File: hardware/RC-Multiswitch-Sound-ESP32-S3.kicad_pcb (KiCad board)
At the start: 2 copper layers, 106 x 68.2 mm, 39 parts, among them CN1 UART A, CN2 3S, CN4 Lautsprecher, J1 Ausgaenge, J11 TPA3118 HW-327, J2 PCM5102A, J5 UART B, J6 UART C, J9 microSD-TF-Modul, U1 ESP32-S3-DevKitC-1 (N16R8), U2 ULN2803A

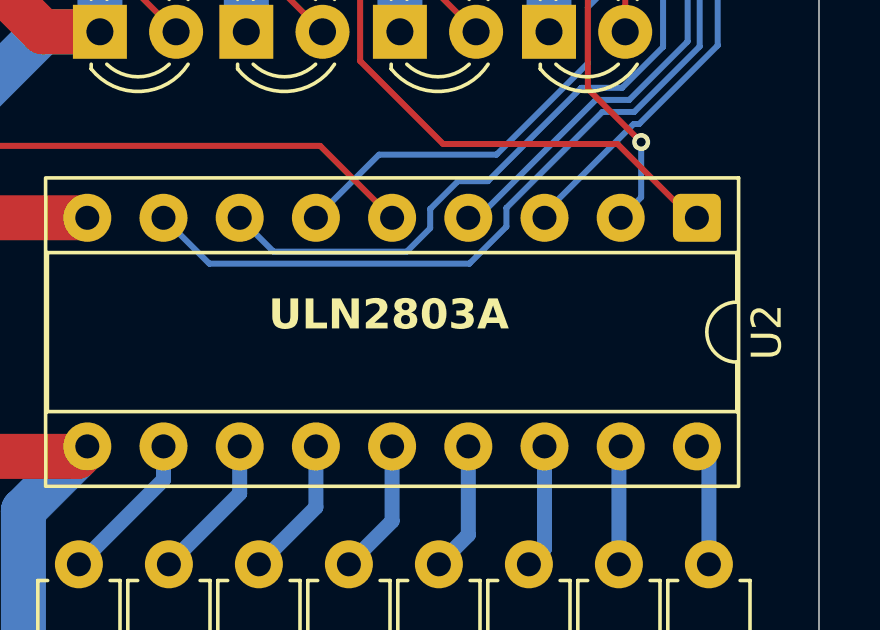
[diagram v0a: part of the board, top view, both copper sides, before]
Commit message: Hardware: TBD62083APG statt ULN2803A
ULN2803A ist abgekuendigt. Der TBD62083APG (DMOS) hat dieselbe Pinbelegung und passt in denselben Sockel, Leiterbahnen und Netze bleiben unveraendert. Schaltplan-Symbol, Bauteilwert, Bestueckungsdruck und Doku angepasst.

Co-Authored-By: Claude Opus 5.5 <noreply@anthropic.com>
Claude-Session: https://claude.ai/code/session_0118D4qppRkb6gR5m3R2CZyV
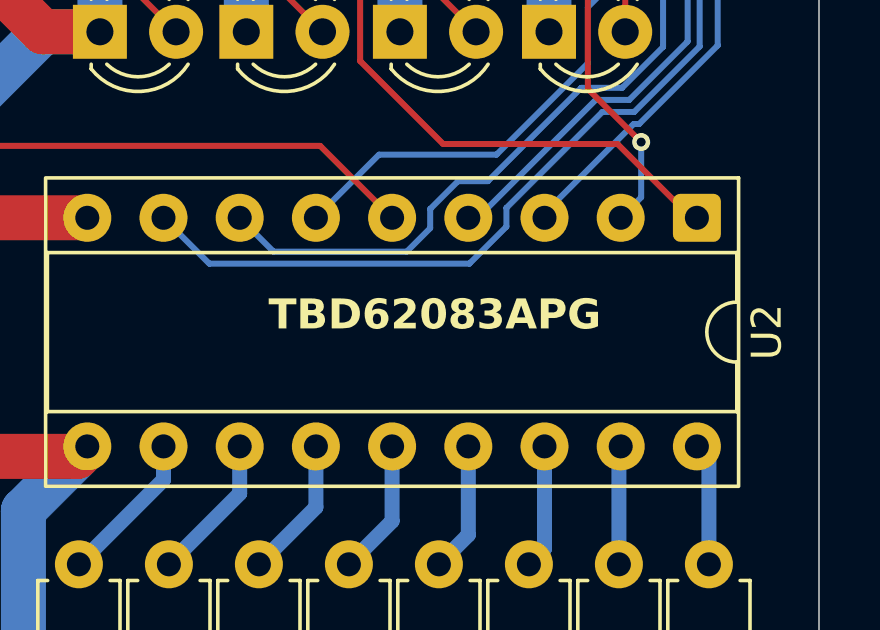
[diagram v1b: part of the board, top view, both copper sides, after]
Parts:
- U2: value ULN2803A -> TBD62083APG
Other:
- board text added: "TBD62083APG"
- board text removed: "ULN2803A"
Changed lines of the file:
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@@
 			)
 		)
-		(property "Value" "ULN2803A"
+		(property "Value" "TBD62083APG"
 			(at 3.4 26.07 90)
 			(layer "F.Fab")
@@
 		)
 	)
-	(gr_text "ULN2803A"
+	(gr_text "TBD62083APG"
 		(at 238.65 122.21 0)
 		(layer "F.SilkS")
